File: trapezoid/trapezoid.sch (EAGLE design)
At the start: 32 parts, among them IC2 LGD20H, U1 MMA8452Q, U2 microSD, U4 MCP73831, Y1 CRYSTAL.ABS25

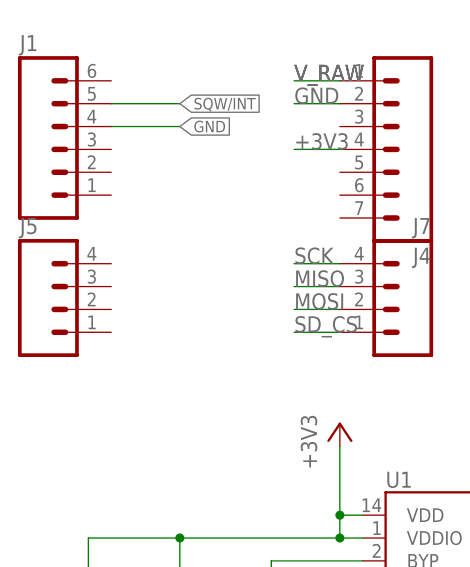
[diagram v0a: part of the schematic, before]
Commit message: changed from 4pin to 3pin header to fit uSD
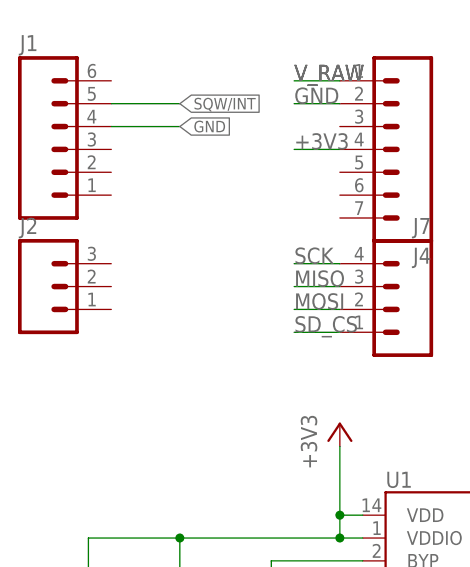
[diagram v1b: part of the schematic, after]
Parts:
- removed J5: (no value), SparkFun-Connectors:M04PTH
- added J2: (no value), SparkFun-Connectors:M03PTH
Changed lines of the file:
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@@
 <part name="GND2" library="SparkFun" deviceset="GND" device=""/>
 <part name="GND3" library="SparkFun" deviceset="GND" device=""/>
-<part name="J5" library="SparkFun-Connectors" deviceset="M04" device="PTH"/>
 <part name="J1" library="SparkFun-Connectors" deviceset="M06" device="SILK_FEMALE_PTH"/>
 <part name="J7" library="SparkFun-Connectors" deviceset="M04" device="PTH"/>
 <part name="J4" library="SparkFun-Connectors" deviceset="M07" device=""/>
+<part name="J2" library="SparkFun-Connectors" deviceset="M03" device="PTH"/>
 </parts>
 <sheets>
@@
 <instance part="GND2" gate="1" x="114.3" y="160.02" rot="R180"/>
 <instance part="GND3" gate="1" x="55.88" y="121.92" rot="R270"/>
-<instance part="J5" gate="G$1" x="7.62" y="60.96"/>
 <instance part="J1" gate="G$1" x="7.62" y="78.74"/>
 <instance part="J7" gate="G$1" x="43.18" y="60.96" rot="MR0"/>
 <instance part="J4" gate="G$1" x="43.18" y="81.28" rot="R180"/>
+<instance part="J2" gate="J$1" x="5.08" y="63.5"/>
 </instances>
 <busses>

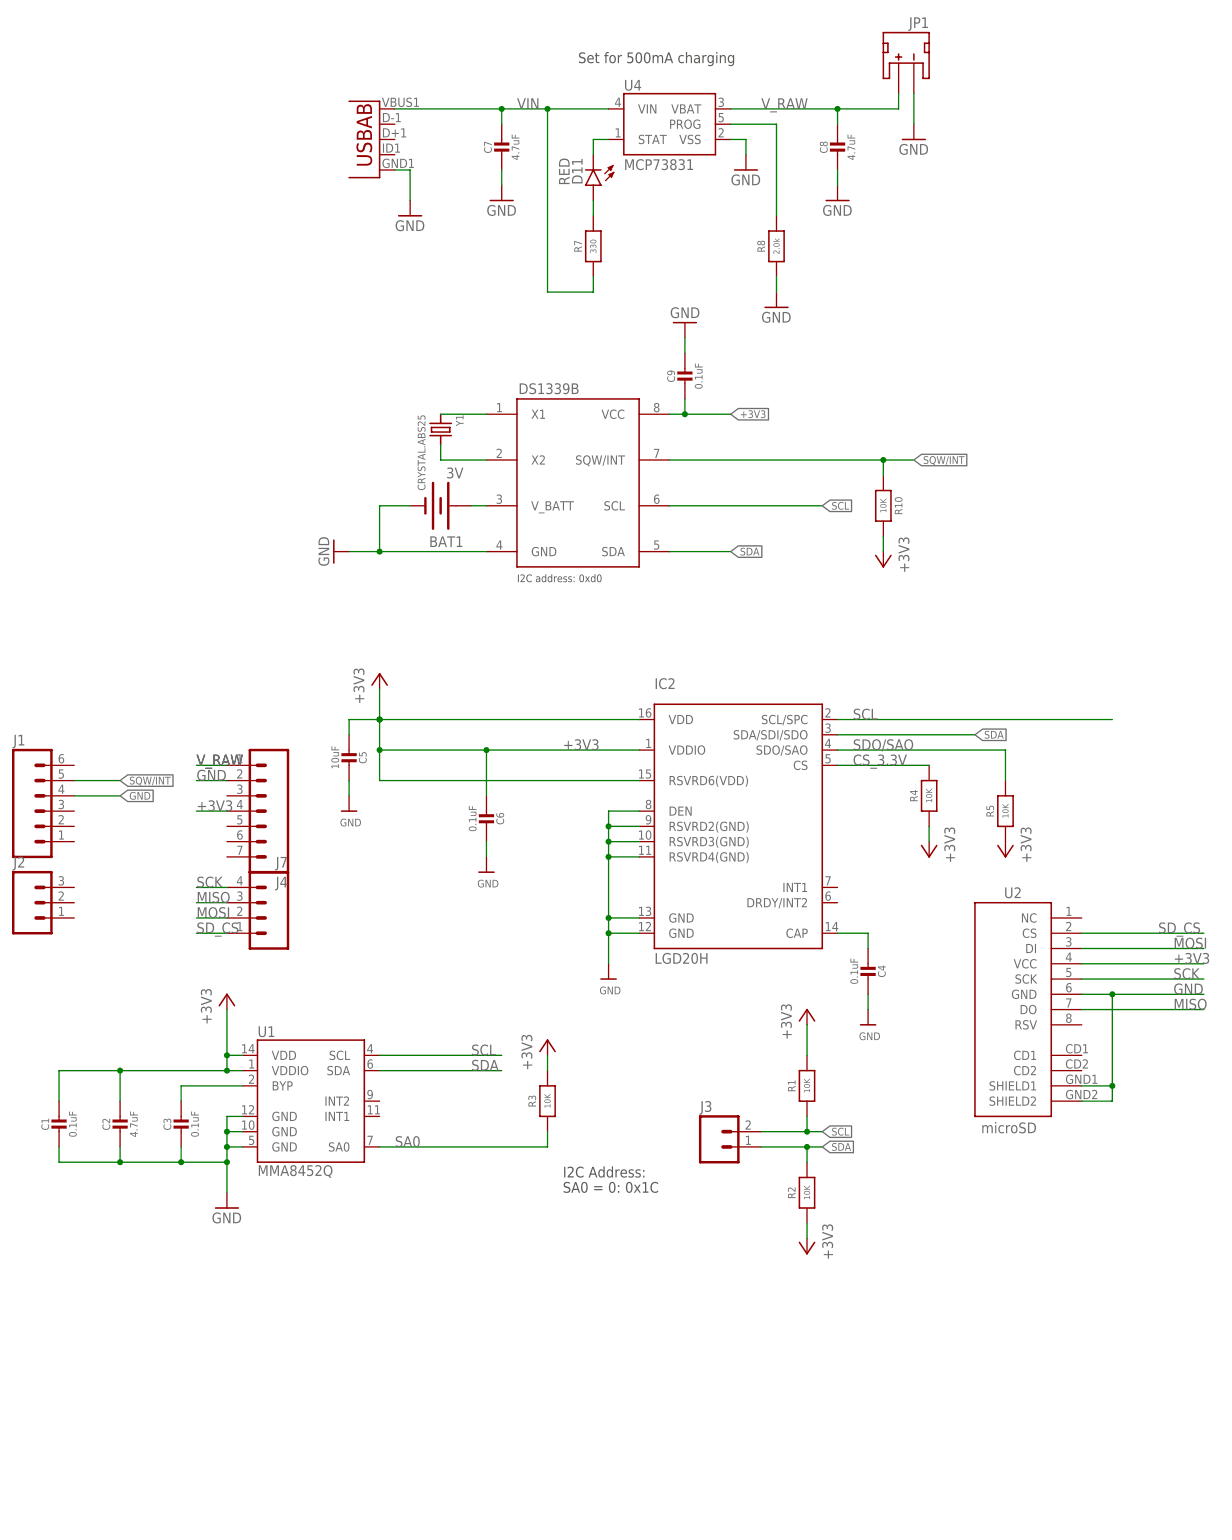
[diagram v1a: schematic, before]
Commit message: changed gyro in schematic
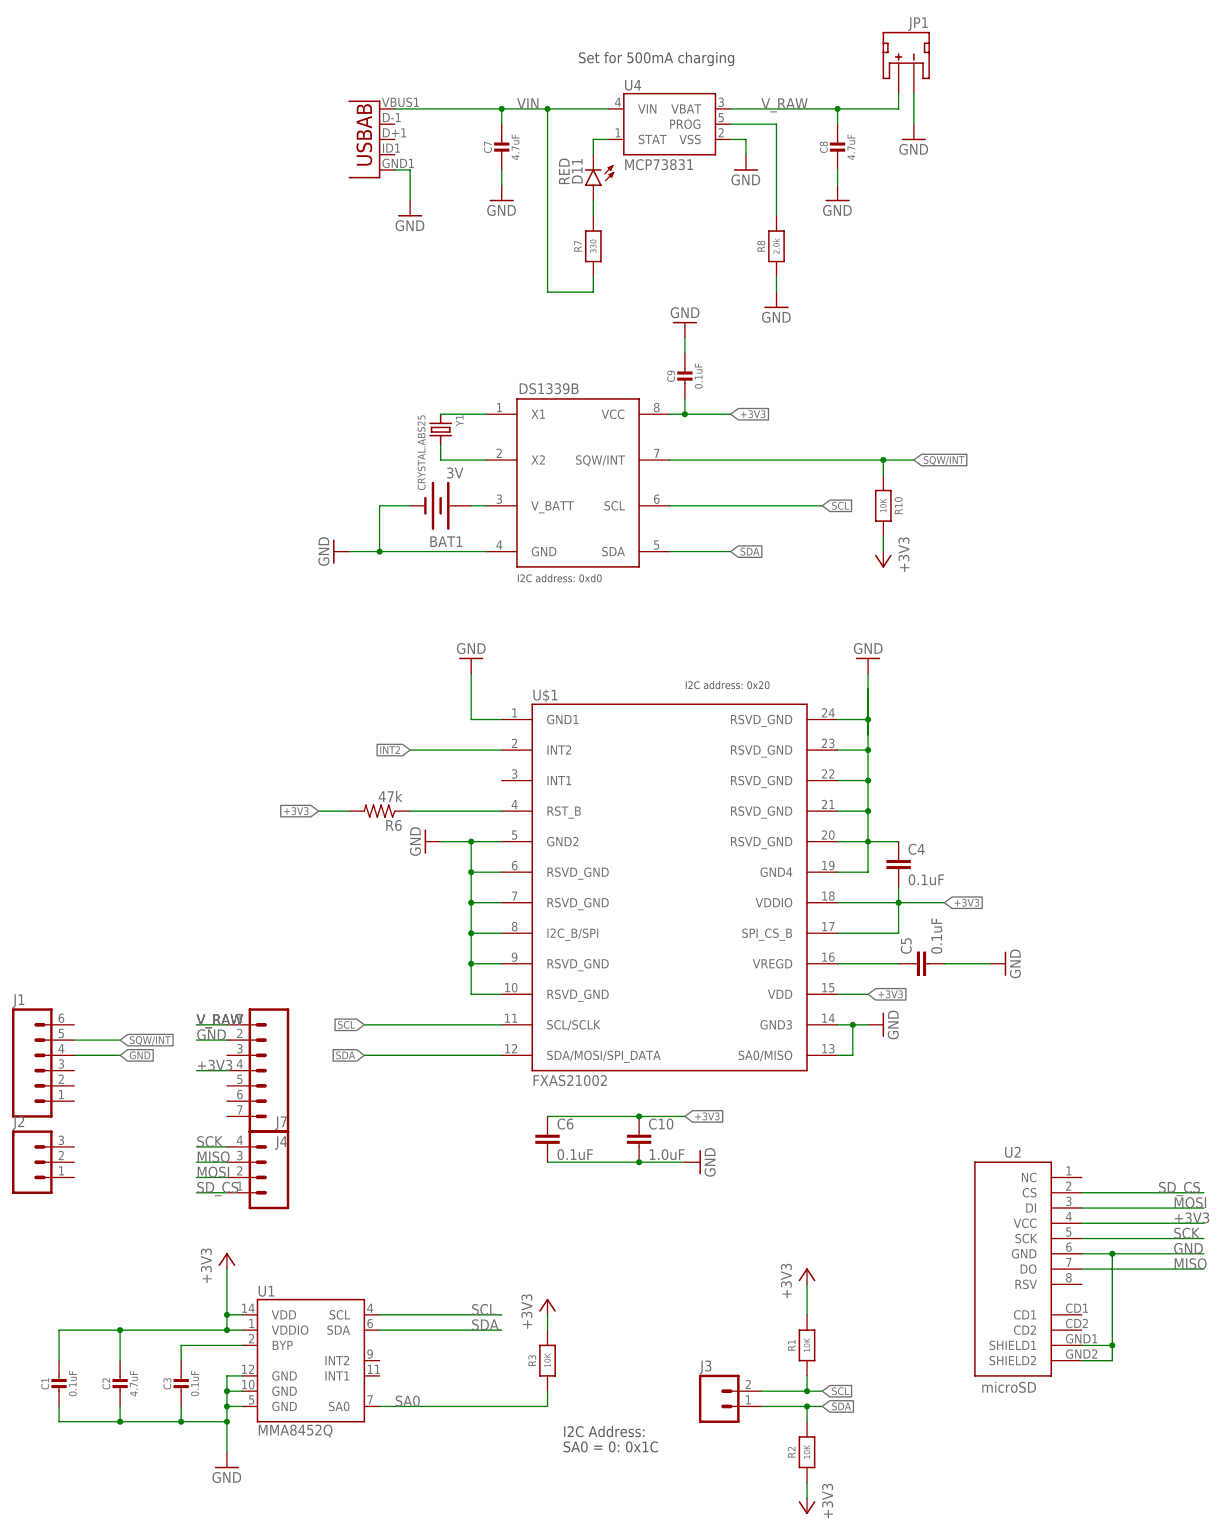
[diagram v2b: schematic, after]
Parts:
- removed IC2: LGD20H, microbuilder:GYRO_L3GD20H
- removed R4, R5: 10K, microbuilder:RESISTOR0805_NOOUTLINE
- added C10: 1.0uF, SparkFun-Passives:CAP0805
- added R6: 47k, SparkFun-Passives:RESISTOR0805-RES
- added U$1: FXAS21002, sharkdunio:FXAS21002
- C4, C6: device microbuilder:CAP_CERAMIC0805-NOOUTLINE -> SparkFun-Passives:CAP0805
- C5: value 10uF -> 0.1uF; device microbuilder:CAP_CERAMIC0805-NOOUTLINE -> SparkFun-Passives:CAP0805
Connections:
- removed net CS_3.3V: IC2.CS, R4.2
- removed net SDO/SAO: IC2.SDO/SAO, R5.2
- new net INT2: U$1.INT2
- new net N$9: R6.1, U$1.RST_B
- net +3V3: now also C10.1, C4.2, C6.1, R6.2, U$1.SPI_CS_B, U$1.VDD, U$1.VDDIO; no longer C5.2, C6.2, IC2.RSVRD6(VDD), IC2.VDD, IC2.VDDIO, R4.1, R5.1
- net GND: now also C10.2, C5.2, C6.2, U$1.GND1, U$1.GND2, U$1.GND3, U$1.GND4, U$1.I2C_B/SPI, U$1.RSVD_GND@1, U$1.RSVD_GND@2, U$1.RSVD_GND@3, U$1.RSVD_GND@4, U$1.RSVD_GND@5, U$1.RSVD_GND@6, U$1.RSVD_GND@7, U$1.RSVD_GND@8, U$1.RSVD_GND@9, U$1.SA0/MISO; no longer C5.1, C6.1, IC2.DEN, IC2.GND@1, IC2.GND@2, IC2.RSVRD2(GND), IC2.RSVRD3(GND), IC2.RSVRD4(GND)
- net N$3: now also C5.1, U$1.VREGD; no longer C4.2, IC2.CAP
- net SCL: now also U$1.SCL/SCLK; no longer IC2.SCL/SPC
- net SDA: now also U$1.SDA/MOSI/SPI_DATA; no longer IC2.SDA/SDI/SDO
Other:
- note added: "I2C address: 0x20"
- moved on the sheet: C1, C2, C3, C4, C5, C6, J1, J2, J3, J4, J7, R1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

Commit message: fully routed board
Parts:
- removed R6: 47k, SparkFun-Passives:RESISTOR0805-RES
- added R4: 47K, microbuilder:RESISTOR0805_NOOUTLINE
- C10: value 1.0uF -> 0.1uF; device SparkFun-Passives:CAP0805 -> microbuilder:CAP_CERAMIC0805-NOOUTLINE
- C4, C5, C6: device SparkFun-Passives:CAP0805 -> microbuilder:CAP_CERAMIC0805-NOOUTLINE
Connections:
- removed net INT2: U$1.INT2
- net +3V3: now also C10.2, C5.2, C6.2, R4.2; no longer C10.1, C4.2, C6.1, R6.2
- net GND: now also C10.1, C4.2, C5.1, C6.1; no longer C10.2, C4.1, C5.2, C6.2
- net N$3: now also C4.1; no longer C5.1
- net N$9: now also R4.1; no longer R6.1
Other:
- moved on the sheet: C10, C4, C5, C6
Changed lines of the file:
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@@
 <part name="U$1" library="sharkdunio" deviceset="FXAS21002" device=""/>
 <part name="GND5" library="SparkFun-Aesthetics" deviceset="GND" device=""/>
-<part name="C4" library="SparkFun-Passives" deviceset="CAP" device="0805" value="0.1uF"/>
-<part name="C5" library="SparkFun-Passives" deviceset="CAP" device="0805" value="0.1uF"/>
 <part name="GND6" library="SparkFun-Aesthetics" deviceset="GND" device=""/>
-<part name="C6" library="SparkFun-Passives" deviceset="CAP" device="0805" value="0.1uF"/>
-<part name="C10" library="SparkFun-Passives" deviceset="CAP" device="0805" value="1.0uF"/>
 <part name="GND7" library="SparkFun-Aesthetics" deviceset="GND" device=""/>
 <part name="GND8" library="SparkFun-Aesthetics" deviceset="GND" device=""/>
-<part name="R6" library="SparkFun-Passives" deviceset="RESISTOR" device="0805-RES" value="47k"/>
 <part name="GND9" library="SparkFun-Aesthetics" deviceset="GND" device=""/>
 <part name="GND10" library="SparkFun-Aesthetics" deviceset="GND" device=""/>
+<part name="R4" library="microbuilder" deviceset="RESISTOR" device="0805_NOOUTLINE" value="47K"/>
+<part name="C10" library="microbuilder" deviceset="CAP_CERAMIC" device="0805-NOOUTLINE" value="0.1uF"/>
+<part name="C4" library="microbuilder" deviceset="CAP_CERAMIC" device="0805-NOOUTLINE" value="0.1uF"/>
+<part name="C5" library="microbuilder" deviceset="CAP_CERAMIC" device="0805-NOOUTLINE" value="0.1uF"/>
+<part name="C6" library="microbuilder" deviceset="CAP_CERAMIC" device="0805-NOOUTLINE" value="0.1uF"/>
 </parts>
 <sheets>
@@
 <instance part="U$1" gate="G$1" x="111.76" y="66.04"/>
 <instance part="GND5" gate="1" x="71.12" y="73.66" rot="R270"/>
-<instance part="C4" gate="G$1" x="149.86" y="68.58"/>
-<instance part="C5" gate="G$1" x="154.94" y="53.34" rot="R90"/>
 <instance part="GND6" gate="1" x="167.64" y="53.34" rot="R90"/>
-<instance part="C6" gate="G$1" x="91.44" y="22.86"/>
-<instance part="C10" gate="G$1" x="106.68" y="22.86"/>
 <instance part="GND7" gate="1" x="116.84" y="20.32" rot="R90"/>
 <instance part="GND8" gate="1" x="147.32" y="43.18" rot="R90"/>
-<instance part="R6" gate="G$1" x="63.5" y="78.74" rot="R180"/>
 <instance part="GND9" gate="1" x="144.78" y="104.14" rot="R180"/>
 <instance part="GND10" gate="1" x="78.74" y="104.14" rot="R180"/>
+<instance part="R4" gate="G$1" x="63.5" y="78.74" rot="R180"/>
+<instance part="C10" gate="G$1" x="149.86" y="68.58"/>
+<instance part="C4" gate="G$1" x="154.94" y="53.34" rot="R90"/>
+<instance part="C5" gate="G$1" x="91.44" y="25.4" rot="R180"/>
+<instance part="C6" gate="G$1" x="106.68" y="25.4" rot="R180"/>
 </instances>
 <busses>
@@
 <wire x1="144.78" y1="68.58" x2="144.78" y2="73.66" width="0.1524" layer="91"/>
 <junction x="144.78" y="73.66"/>
-<pinref part="C4" gate="G$1" pin="1"/>
 <wire x1="149.86" y1="73.66" x2="144.78" y2="73.66" width="0.1524" layer="91"/>
 <pinref part="GND9" gate="1" pin="GND"/>
+<pinref part="C10" gate="G$1" pin="1"/>
 </segment>
 <segment>
@@
 </segment>
 <segment>
-<pinref part="C5" gate="G$1" pin="2"/>
 <wire x1="157.48" y1="53.34" x2="165.1" y2="53.34" width="0.1524" layer="91"/>
 <pinref part="GND6" gate="1" pin="GND"/>
-</segment>
-<segment>
-<pinref part="C6" gate="G$1" pin="2"/>
-<pinref part="C10" gate="G$1" pin="2"/>
+<pinref part="C4" gate="G$1" pin="2"/>
+</segment>
+<segment>
 <wire x1="91.44" y1="20.32" x2="106.68" y2="20.32" width="0.1524" layer="91"/>
 <pinref part="GND7" gate="1" pin="GND"/>
-<wire x1="114.3" y1="20.32" x2="106.68" y2="20.32" width="0.1524" layer="91"/>
+<pinref part="C5" gate="G$1" pin="1"/>
+<pinref part="C6" gate="G$1" pin="1"/>
+<wire x1="106.68" y1="20.32" x2="114.3" y2="20.32" width="0.1524" layer="91"/>
 <junction x="106.68" y="20.32"/>
 </segment>
@@
 <segment>
 <pinref part="U$1" gate="G$1" pin="SCL/SCLK"/>
-<wire x1="83.82" y1="43.18" x2="60.96" y2="43.18" width="0.1524" layer="91"/>
-<label x="60.96" y="43.18" size="1.27" layer="95" rot="R180" xref="yes"/>
+<wire x1="83.82" y1="43.18" x2="71.12" y2="43.18" width="0.1524" layer="91"/>
+<label x="71.12" y="43.18" size="1.27" layer="95" rot="R180" xref="yes"/>
 </segment>
 </net>
@@
 <segment>
 <pinref part="U$1" gate="G$1" pin="SDA/MOSI/SPI_DATA"/>
-<wire x1="83.82" y1="38.1" x2="60.96" y2="38.1" width="0.1524" layer="91"/>
-<label x="60.96" y="38.1" size="1.27" layer="95" rot="R180" xref="yes"/>
+<wire x1="83.82" y1="38.1" x2="71.12" y2="38.1" width="0.1524" layer="91"/>
+<label x="71.12" y="38.1" size="1.27" layer="95" rot="R180" xref="yes"/>
 </segment>
 </net>
@@
 <pinref part="U$1" gate="G$1" pin="VDDIO"/>
 <wire x1="139.7" y1="63.5" x2="149.86" y2="63.5" width="0.1524" layer="91"/>
-<pinref part="C4" gate="G$1" pin="2"/>
 <wire x1="149.86" y1="63.5" x2="149.86" y2="66.04" width="0.1524" layer="91"/>
 <wire x1="149.86" y1="63.5" x2="157.48" y2="63.5" width="0.1524" layer="91"/>
@@
 <wire x1="149.86" y1="58.42" x2="149.86" y2="63.5" width="0.1524" layer="91"/>
 <label x="157.48" y="63.5" size="1.27" layer="95" xref="yes"/>
-</segment>
-<segment>
-<pinref part="C10" gate="G$1" pin="1"/>
-<pinref part="C6" gate="G$1" pin="1"/>
+<pinref part="C10" gate="G$1" pin="2"/>
+</segment>
+<segment>
+<wire x1="114.3" y1="27.94" x2="106.68" y2="27.94" width="0.1524" layer="91"/>
+<label x="114.3" y="27.94" size="1.27" layer="95" xref="yes"/>
+<pinref part="C5" gate="G$1" pin="2"/>
+<pinref part="C6" gate="G$1" pin="2"/>
 <wire x1="106.68" y1="27.94" x2="91.44" y2="27.94" width="0.1524" layer="91"/>
-<wire x1="106.68" y1="27.94" x2="114.3" y2="27.94" width="0.1524" layer="91"/>
 <junction x="106.68" y="27.94"/>
-<label x="114.3" y="27.94" size="1.27" layer="95" xref="yes"/>
 </segment>
 <segment>
@@
 </segment>
 <segment>
-<pinref part="R6" gate="G$1" pin="2"/>
 <wire x1="58.42" y1="78.74" x2="53.34" y2="78.74" width="0.1524" layer="91"/>
 <label x="53.34" y="78.74" size="1.27" layer="95" rot="R180" xref="yes"/>
+<pinref part="R4" gate="G$1" pin="2"/>
 </segment>
 </net>
@@
 <segment>
 <pinref part="U$1" gate="G$1" pin="VREGD"/>
-<pinref part="C5" gate="G$1" pin="1"/>
 <wire x1="139.7" y1="53.34" x2="149.86" y2="53.34" width="0.1524" layer="91"/>
+<pinref part="C4" gate="G$1" pin="1"/>
 </segment>
 </net>
@@
 <pinref part="U$1" gate="G$1" pin="RST_B"/>
 <wire x1="83.82" y1="78.74" x2="68.58" y2="78.74" width="0.1524" layer="91"/>
-<pinref part="R6" gate="G$1" pin="1"/>
-</segment>
-</net>
-<net name="INT2" class="0">
-<segment>
-<pinref part="U$1" gate="G$1" pin="INT2"/>
-<wire x1="83.82" y1="88.9" x2="68.58" y2="88.9" width="0.1524" layer="91"/>
-<label x="68.58" y="88.9" size="1.27" layer="95" rot="R180" xref="yes"/>
-</segment>
-</net>
+<pinref part="R4" gate="G$1" pin="1"/>
+</segment>
+</net>

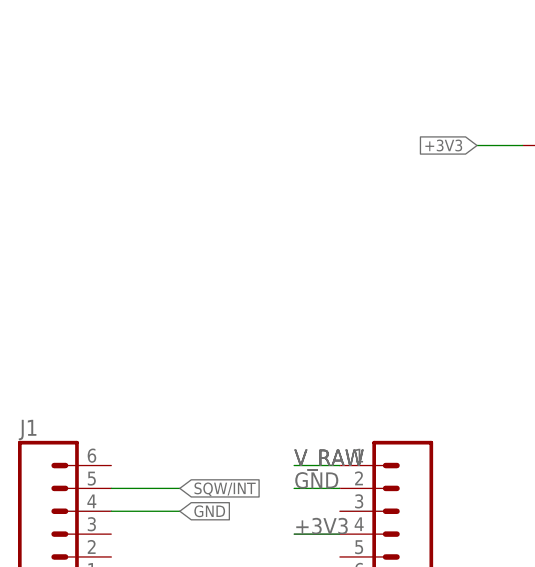
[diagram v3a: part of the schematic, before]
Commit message: add raw voltage headers
allow for easy attachment of inductive charging
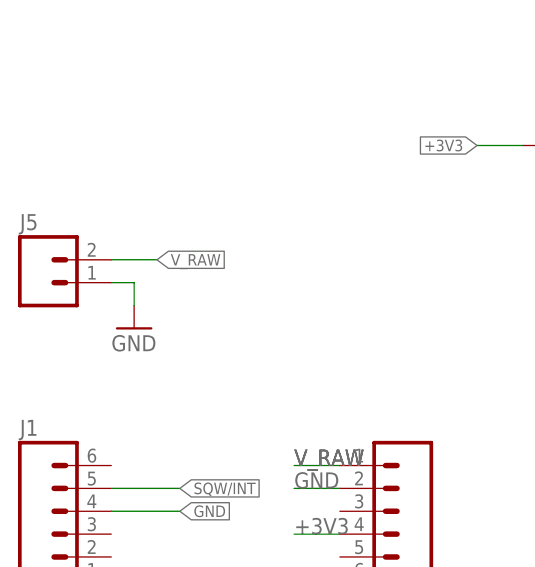
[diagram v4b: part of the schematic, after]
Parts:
- added J5: (no value), SparkFun-Connectors:M02LOCK
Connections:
- net GND: now also J5.1
- net V_RAW: now also J5.2
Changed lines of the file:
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@@
 <part name="C5" library="microbuilder" deviceset="CAP_CERAMIC" device="0805-NOOUTLINE" value="0.1uF"/>
 <part name="C6" library="microbuilder" deviceset="CAP_CERAMIC" device="0805-NOOUTLINE" value="0.1uF"/>
+<part name="J5" library="SparkFun-Connectors" deviceset="M02" device="LOCK"/>
+<part name="GND11" library="SparkFun-Aesthetics" deviceset="GND" device=""/>
 </parts>
 <sheets>
@@
 <instance part="C5" gate="G$1" x="91.44" y="25.4" rot="R180"/>
 <instance part="C6" gate="G$1" x="106.68" y="25.4" rot="R180"/>
+<instance part="J5" gate="G$1" x="5.08" y="63.5"/>
+<instance part="GND11" gate="1" x="15.24" y="58.42"/>
 </instances>
 <busses>
@@
 <wire x1="144.78" y1="91.44" x2="144.78" y2="99.06" width="0.1524" layer="91"/>
 </segment>
+<segment>
+<pinref part="J5" gate="G$1" pin="1"/>
+<wire x1="12.7" y1="63.5" x2="15.24" y2="63.5" width="0.1524" layer="91"/>
+<pinref part="GND11" gate="1" pin="GND"/>
+<wire x1="15.24" y1="63.5" x2="15.24" y2="60.96" width="0.1524" layer="91"/>
+</segment>
 </net>
 <net name="SCL" class="0">
@@
 <pinref part="C8" gate="G$1" pin="1"/>
 </segment>
-</net>
+<segment>
+<pinref part="J5" gate="G$1" pin="2"/>
+<wire x1="12.7" y1="66.04" x2="17.78" y2="66.04" width="0.1524" layer="91"/>
+<label x="17.78" y="66.04" size="1.27" layer="95" xref="yes"/>
+</segment>
+</net>
